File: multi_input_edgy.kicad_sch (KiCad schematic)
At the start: 10 parts, among them J1 002, J2 002, J7 6V-24V, U18 SN74LVC1G125

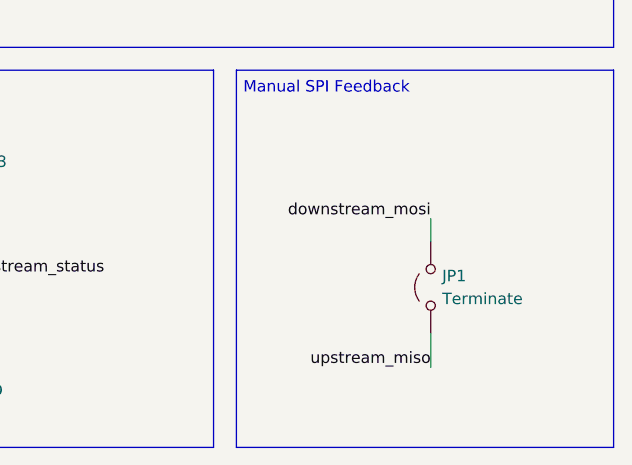
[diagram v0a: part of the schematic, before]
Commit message: Get board name and version from text variable
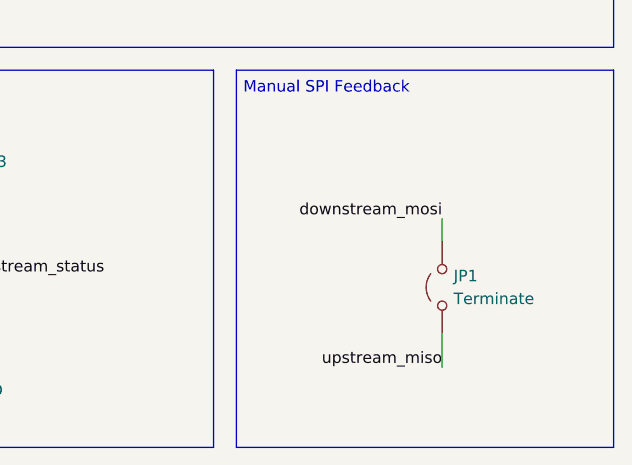
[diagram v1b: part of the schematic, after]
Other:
- title: (none) -> ${BoardName}
- moved on the sheet: JP1
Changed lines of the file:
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@@
 	(generator_version "8.99")
 	(paper "A4")
+	(title_block
+		(title "${BoardName}")
+		(date "2024-11-11")
+		(rev "${Version}")
+	)
 	(rectangle
 		(start 109.728 107.95)
@@
 	(wire
 		(pts
-			(xy 209.55 137.16) (xy 209.55 140.97)
+			(xy 210.82 137.16) (xy 210.82 140.97)
 		)
 		(stroke
@@
 	(wire
 		(pts
-			(xy 209.55 124.46) (xy 209.55 127)
+			(xy 210.82 124.46) (xy 210.82 127)
 		)
 		(stroke
@@
 	)
 	(label "upstream_miso"
-		(at 209.55 140.97 180)
+		(at 210.82 140.97 180)
 		(fields_autoplaced yes)
 		(effects
@@
 	)
 	(label "downstream_mosi"
-		(at 209.55 124.46 180)
+		(at 210.82 124.46 180)
 		(fields_autoplaced yes)
 		(effects
@@
 	(symbol
 		(lib_id "Jumper:Jumper_2_Open")
-		(at 209.55 132.08 90)
+		(at 210.82 132.08 90)
 		(unit 1)
 		(exclude_from_sim yes)
@@
 		(dnp no)
 		(property "Reference" "JP1"
-			(at 210.82 130.8099 90)
+			(at 212.09 130.8099 90)
 			(effects
 				(font
@@
 		)
 		(property "Value" "Terminate"
-			(at 210.82 133.3499 90)
+			(at 212.09 133.3499 90)
 			(effects
 				(font
@@
 		)
 		(property "Footprint" "Connector_PinHeader_2.54mm:PinHeader_1x02_P2.54mm_Vertical"
-			(at 209.55 132.08 0)
+			(at 210.82 132.08 0)
 			(effects
 				(font
@@
 		)
 		(property "Datasheet" "~"
-			(at 209.55 132.08 0)
+			(at 210.82 132.08 0)
 			(effects
 				(font
@@
 		)
 		(property "Description" "Jumper, 2-pole, open"
-			(at 209.55 132.08 0)
+			(at 210.82 132.08 0)
 			(effects
 				(font
@@
 		)
 		(property "Text" ""
-			(at 209.55 132.08 0)
+			(at 210.82 132.08 0)
 			(effects
 				(font

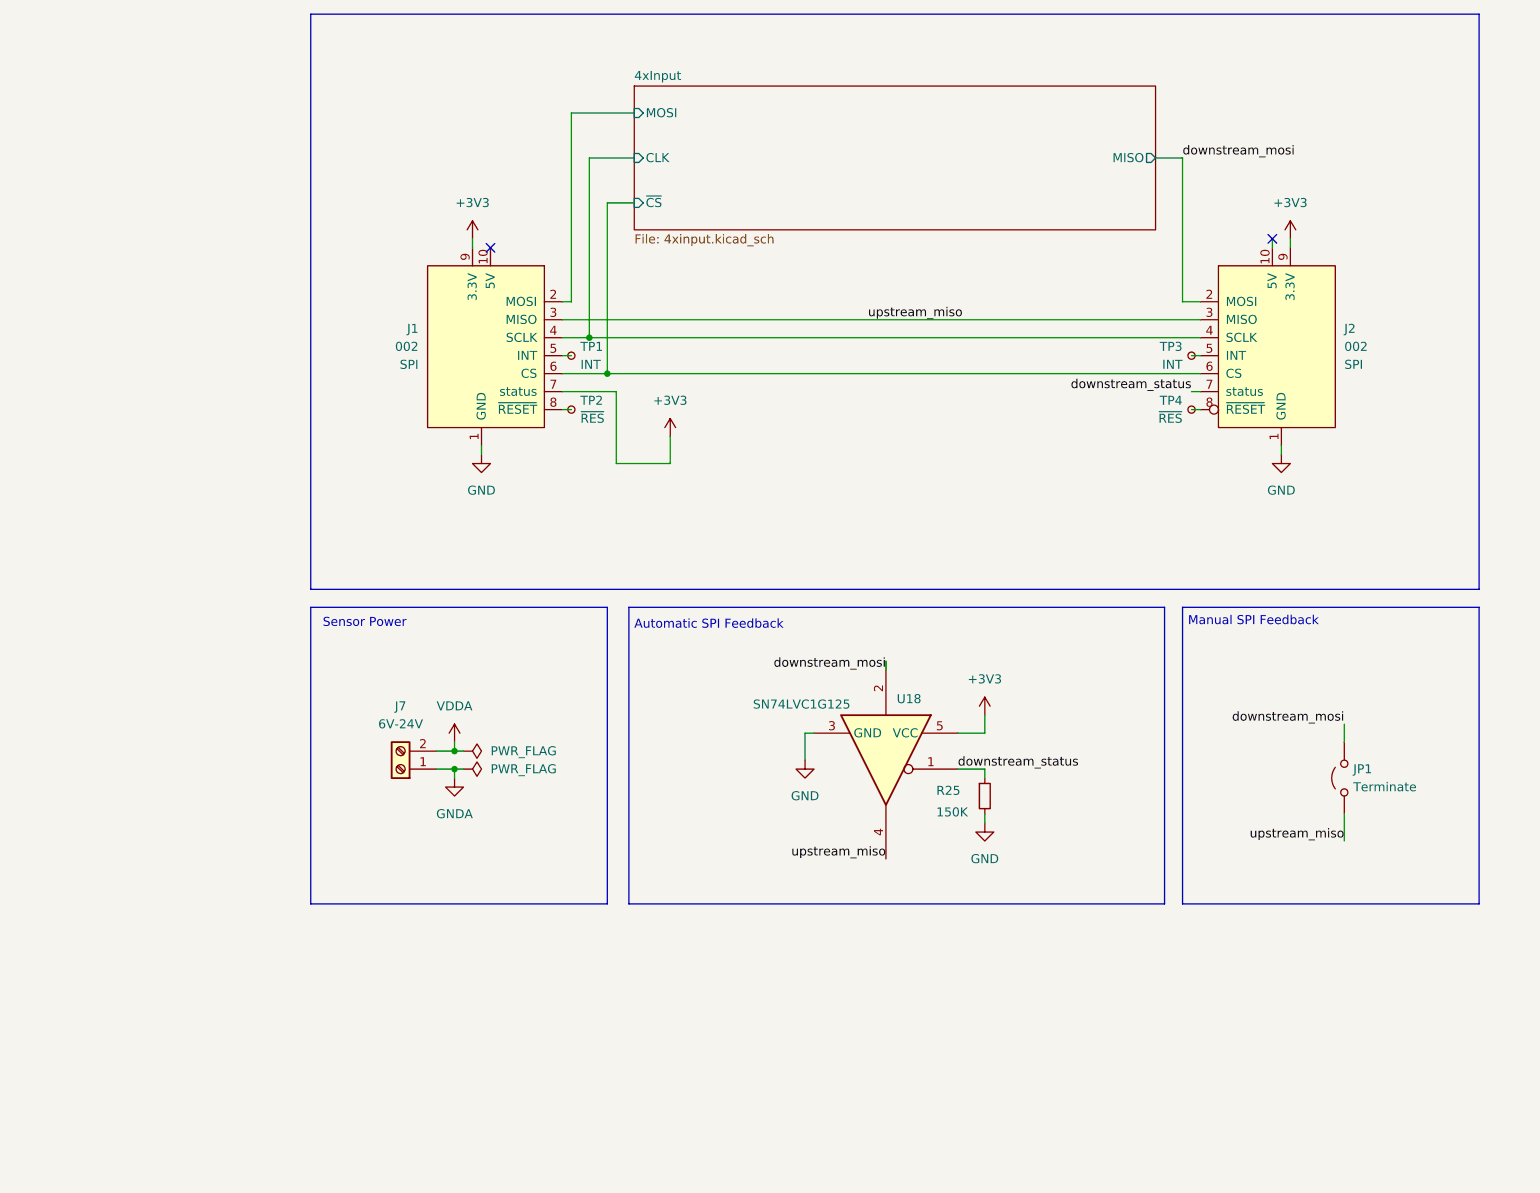
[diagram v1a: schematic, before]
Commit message: Change optocouplers, improve power routing
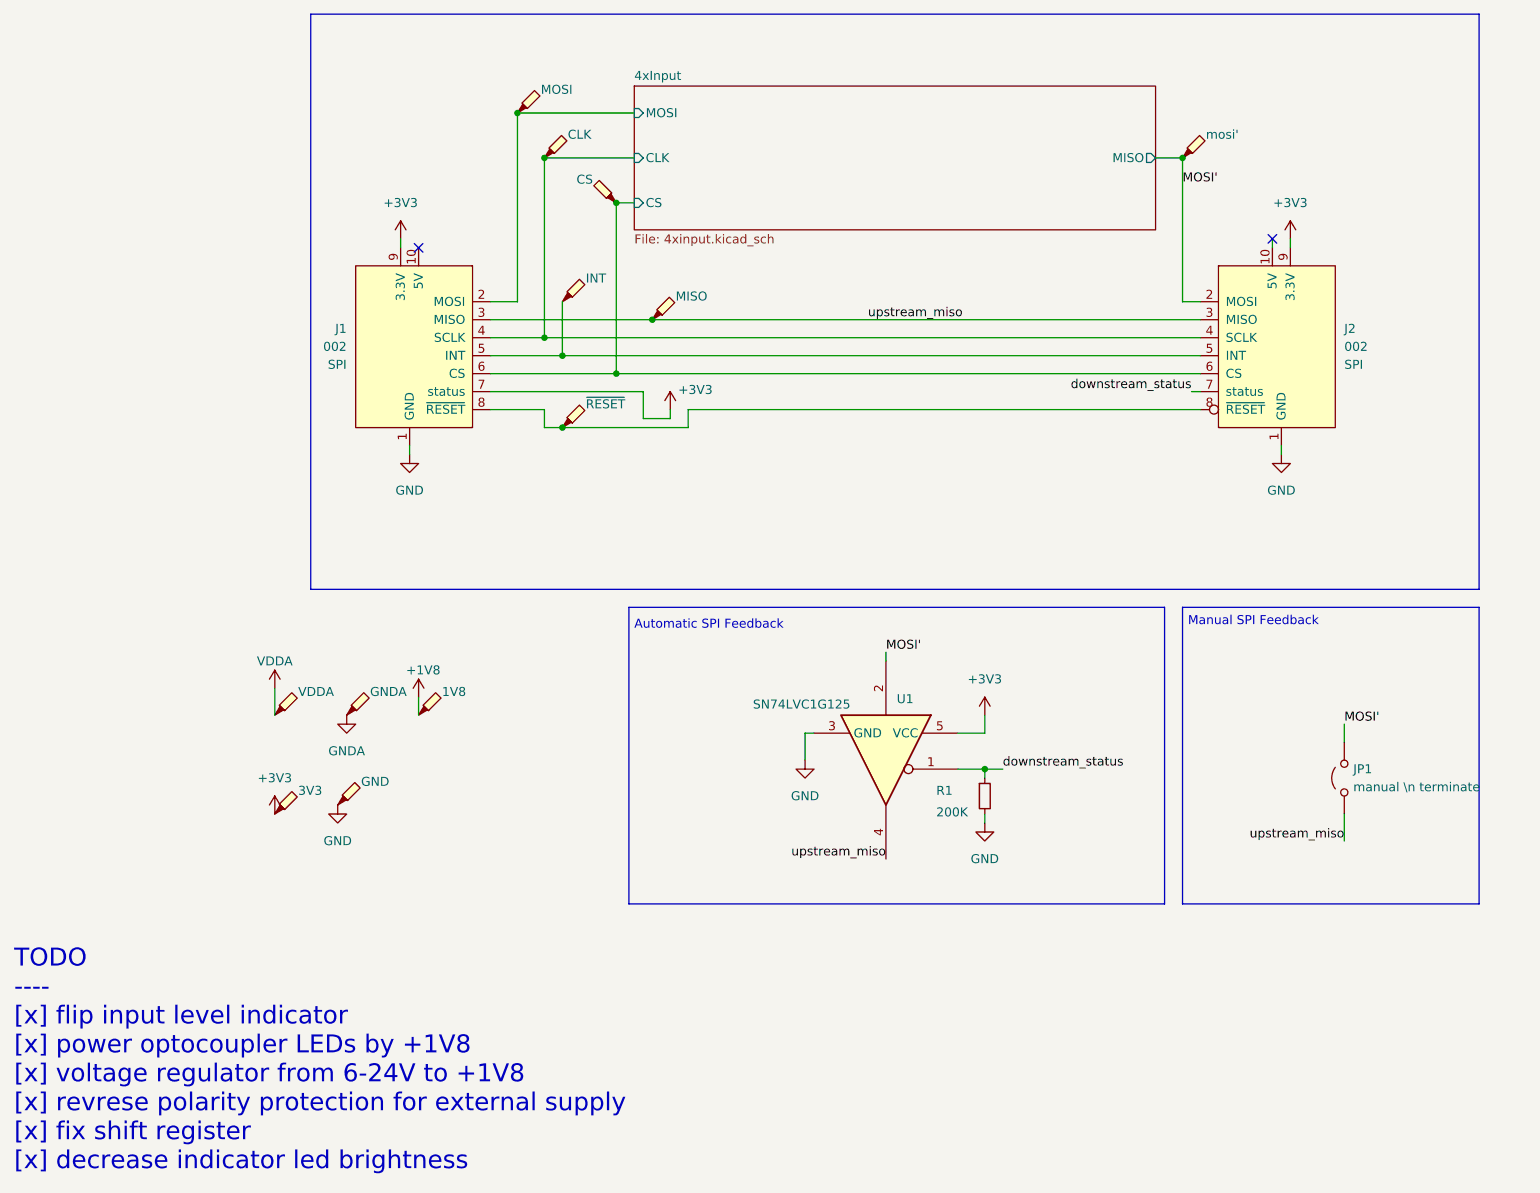
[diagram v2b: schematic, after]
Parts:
- removed J7: 6V-24V, Connector_Molex:Molex_KK-254_AE-6410-02A_1x02_P2.54mm_Vertical, symbol Connector:Screw_Terminal_01x02
- removed TP1, TP3: INT, TestPoint:TestPoint_THTPad_D1.0mm_Drill0.5mm, symbol Connector:TestPoint_Small
- removed TP2, TP4: ~{RES}, TestPoint:TestPoint_THTPad_D1.0mm_Drill0.5mm, symbol Connector:TestPoint_Small
- added TP10: MISO, TestPoint:TestPoint_THTPad_D1.0mm_Drill0.5mm, symbol Connector:TestPoint_Probe
- added TP11: mosi', TestPoint:TestPoint_THTPad_D1.0mm_Drill0.5mm, symbol Connector:TestPoint_Probe
- added TP12: CS, TestPoint:TestPoint_THTPad_D1.0mm_Drill0.5mm, symbol Connector:TestPoint_Probe
- added TP13: 3V3, TestPoint:TestPoint_THTPad_D1.0mm_Drill0.5mm, symbol Connector:TestPoint_Probe
- added TP14: GND, TestPoint:TestPoint_THTPad_D1.0mm_Drill0.5mm, symbol Connector:TestPoint_Probe
- added TP15: VDDA, TestPoint:TestPoint_THTPad_D1.0mm_Drill0.5mm, symbol Connector:TestPoint_Probe
- added TP16: GNDA, TestPoint:TestPoint_THTPad_D1.0mm_Drill0.5mm, symbol Connector:TestPoint_Probe
- added TP17: 1V8, TestPoint:TestPoint_THTPad_D1.0mm_Drill0.5mm, symbol Connector:TestPoint_Probe
- added TP6: MOSI, TestPoint:TestPoint_THTPad_D1.0mm_Drill0.5mm, symbol Connector:TestPoint_Probe
- added TP7: CLK, TestPoint:TestPoint_THTPad_D1.0mm_Drill0.5mm, symbol Connector:TestPoint_Probe
- added TP8: INT, TestPoint:TestPoint_THTPad_D1.0mm_Drill0.5mm, symbol Connector:TestPoint_Probe
- added TP9: ~{RESET}, TestPoint:TestPoint_THTPad_D1.0mm_Drill0.5mm, symbol Connector:TestPoint_Probe
- JP1: value Terminate -> manual \n terminate
- R1: renamed from R25; value 150K -> 200K; LCSC Part# C25755 -> C25764
- renumbered U18 to U1
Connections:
- net +3V3: now also TP13.1
- net 4xInput/CLK: now also TP7.1
- net 4xInput/MOSI: now also TP6.1
- net GND: now also TP14.1
- net GNDA: now also TP16.1
- net VDDA: now also TP15.1
- net upstream_miso: now also TP10.1
- net at J1.5 (INT): now also J2.5 (INT), TP8.1
- net at J1.8 (~{RESET}): now also J2.8 (~{RESET}), TP9.1
- net 4xInput/~{CS} renamed 4xInput/CS
- net 4xInput/CS: now also TP12.1
- net downstream_mosi renamed MOSI'
- net MOSI': now also TP11.1
- new net +1V8: TP17.1
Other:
- sheet 4xInput ports: added CS; removed ~{CS}
- note added: "TODO ---- [x] flip input level indicator [x] power optocoupler LEDs by +1V8 [x] voltage regulator from 6-24V to +1V8 [x] revrese polarity protection for external supply [x] fix shift register [x] decrease indicator led brightness"
- note removed: "Sensor Power"
- moved on the sheet: J1
